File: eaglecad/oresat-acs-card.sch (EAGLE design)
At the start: 287 parts, among them J6 J-SAMTEC-TFM-120-X1-XXX-D-RA, Q10 DMP2240UDM, Q11 MOSFET-PCH-SOT23-6, Q12 MOSFET-PCH-SOT23-6, Q13 PMV45EN, Q14 PMV45EN, Q15 DMP2240UDM, Q21 MOSFET-PCH-SOT23-6, Q22 MOSFET-PCH-SOT23-6, Q23 PMV45EN, Q24 PMV45EN, Q25 DMP2240UDM, Q31 MOSFET-PCH-SOT23-6, Q32 MOSFET-PCH-SOT23-6, Q33 PMV45EN, Q34 PMV45EN, Q35 DMP2240UDM, Q6 MOSFET-PCH-SOT23-6, Q7 MOSFET-PCH-SOT23-6, Q8 PMV45EN, Q9 PMV45EN, U10 MAX4211FETE, U11 MIC842LYC5, U12 MIC842LYC5, U17 MAX7310ATE, U18 MAX4211FETE, U19 MIC842LYC5, U20 MIC842LYC5, U25 MAX7310ATE, U26 MAX4211FETE, U27 MIC842LYC5, U28 MIC842LYC5, U5 MAX7310ATE, U6 MAX4211FETE, U7 MIC842LYC5, U8 MIC842LYC5, U9 MAX7310ATE

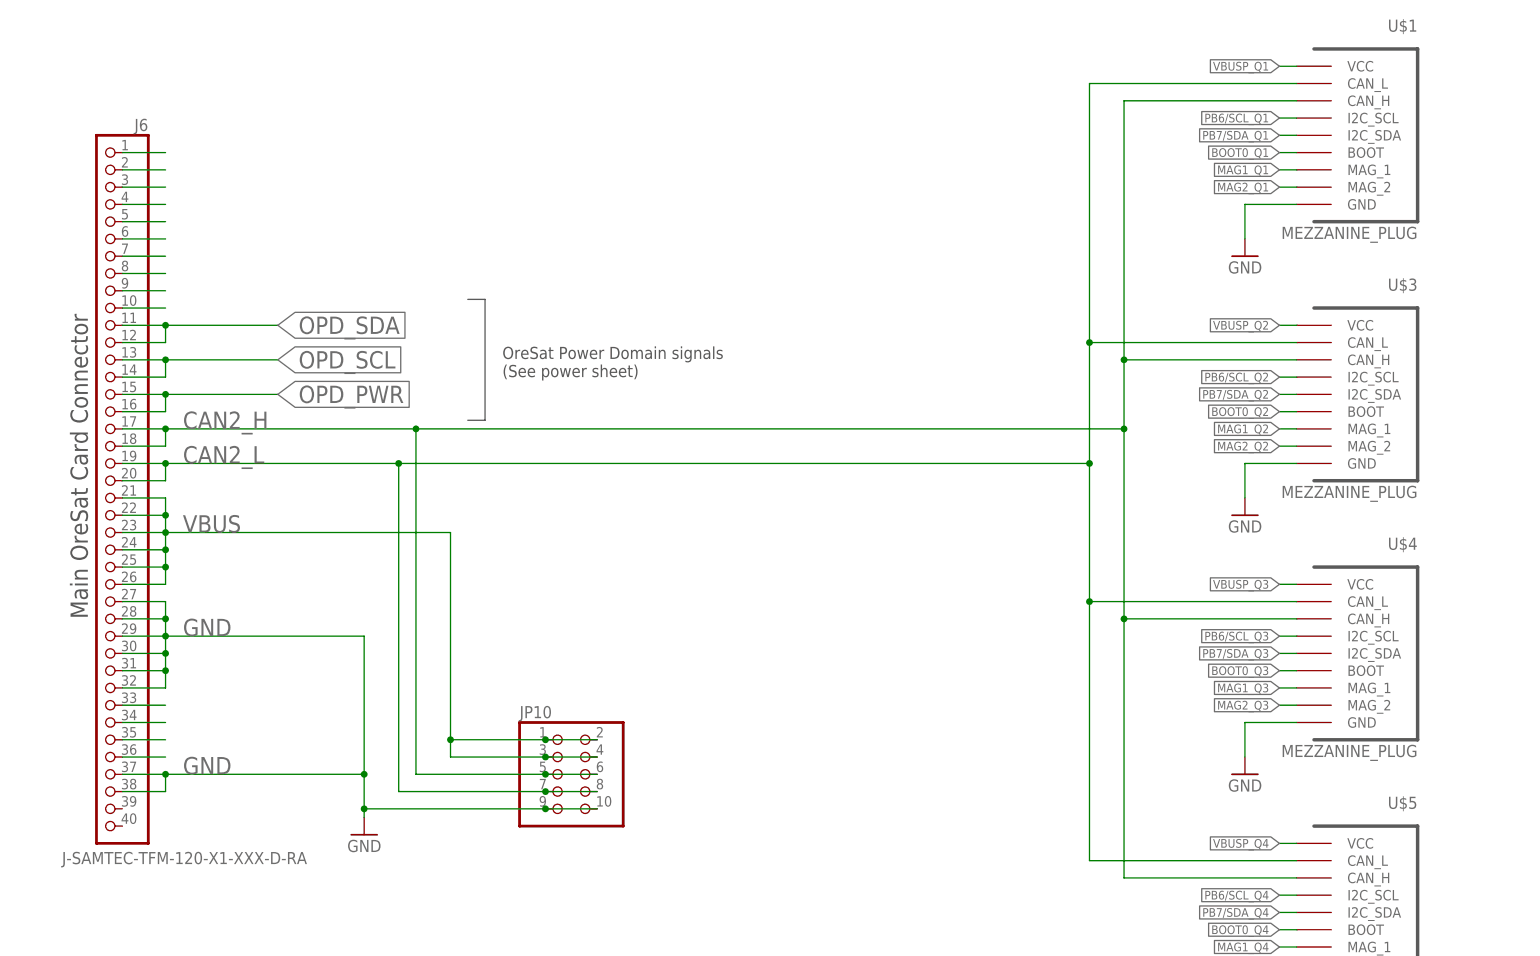
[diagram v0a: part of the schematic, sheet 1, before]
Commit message: Sanity check Eric's card. Removing supply symbols even though this is causing Andrew physical pain but EAGLE can't deal with renaming supply symbols. Also more text.
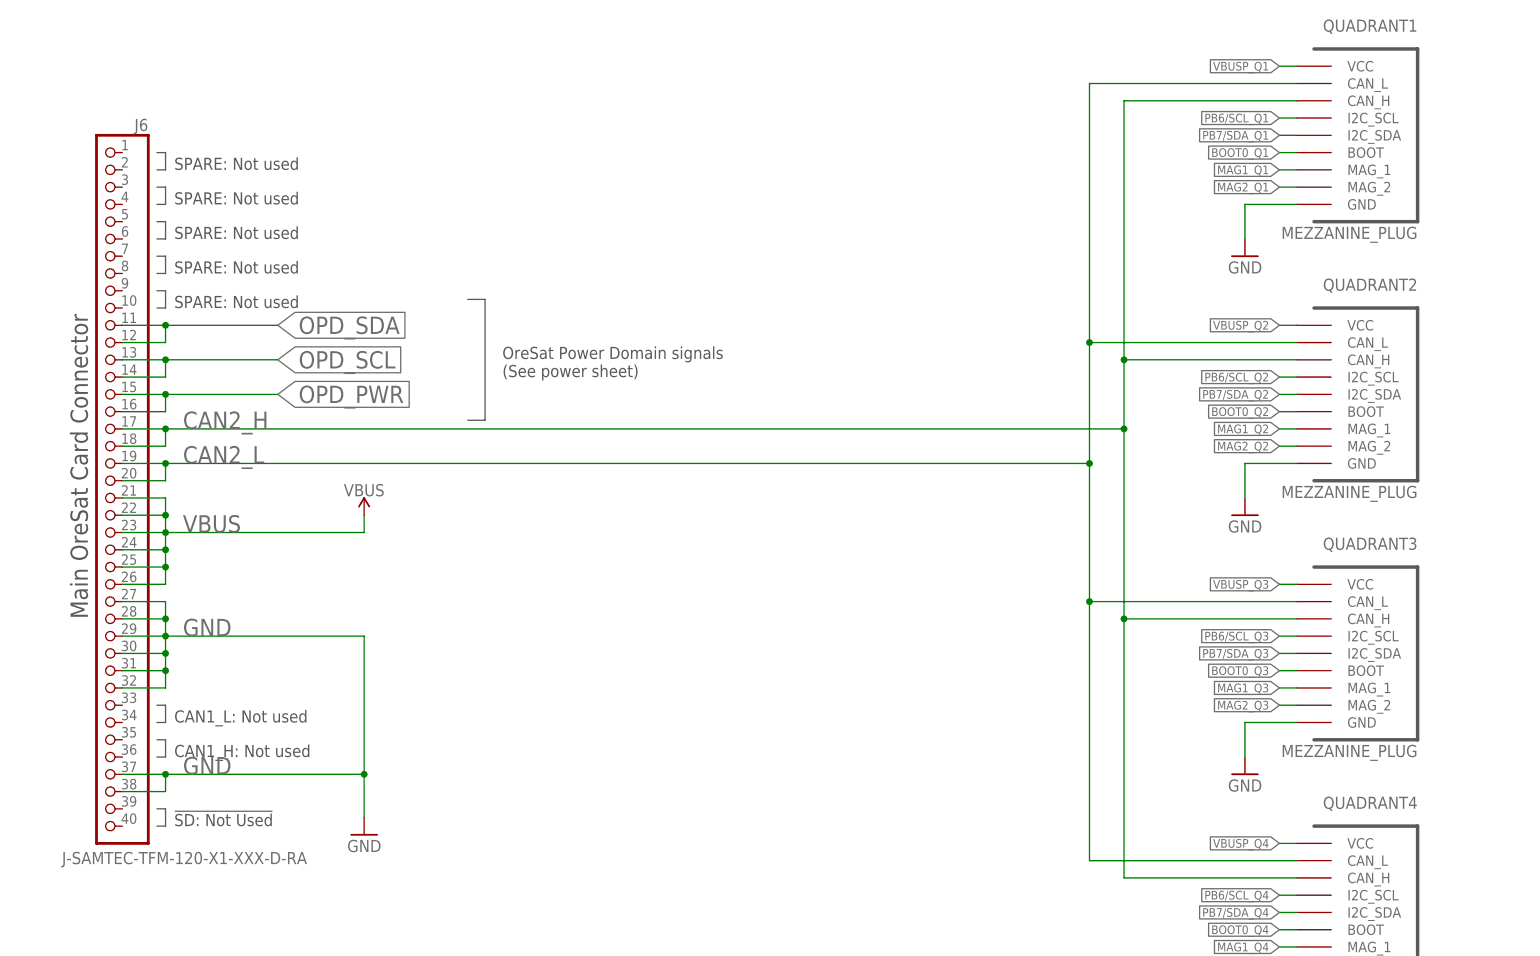
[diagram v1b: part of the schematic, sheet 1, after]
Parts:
- removed JP10: (no value), pinhead:PINHD-2X5
- renumbered U$1 to QUADRANT1, U$3 to QUADRANT2, U$4 to QUADRANT3, U$5 to QUADRANT4
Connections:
- removed net N$1: J6.34
- removed net N$271: J6.33
- removed net N$300: J6.2
- removed net N$400: J6.35
- removed net N$406: J6.36
- removed net N$479: J6.9
- removed net N$480: J6.4
- removed net N$482: J6.5
- removed net N$498: J6.1
- removed net N$499: J6.7
- removed net N$500: J6.6
- removed net N$503: J6.8
- removed net N$504: J6.10
- removed net SPARE4: J6.3
- net CAN2_H: no longer JP10.5, JP10.6
- net CAN2_L: no longer JP10.7, JP10.8
- net GND: no longer JP10.10, JP10.9
- net VBUS: no longer JP10.1, JP10.2, JP10.3, JP10.4
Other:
- note added: "!SD: Not Used"
- note added: "CAN1_H: Not used"
- note added: "CAN1_L: Not used"
- note added: "SPARE: Not used"

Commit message: Layed out power domains for four quadrants, added another power domain and an STM32F042. Also added breaker circuit and I2C buffer for Magnetometers, and an IMU
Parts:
- added C1, C16, C2, C3, C4, C46, C48, C49, C50: 1u, oresat-rcl:C-EU0603-C-NOSILK
- added C18, C26, C27, C43, C5: 100n, oresat-rcl:C-EU0603-C-NOSILK
- added C19, C20: 20p, oresat-rcl:C-EU0603-C-NOSILK
- added C44: NP, oresat-rcl:C-EU0603-C-NOSILK
- added C45: 10u, oresat-rcl:C-EU0805-B-NOSILK
- added C47: 22u, oresat-rcl:C-EU0805-B-NOSILK
- added D16, D17: GREEN, SparkFun-LED:LED-GREEN0603
- added D18, D2: AMBER, SparkFun-LED:LED-GREEN0603
- added J2: ORESAT-DEBUG-CONNECTOR-CARD, oresat-edge_connector:ORESAT-DEBUG-CONNECTOR-CARD
- added L3: 6.8u, L-ECS-MPI4040:L-ECS-MPI4040
- added MAG_PIN_Q1, MAG_PIN_Q2, MAG_PIN_Q3, MAG_PIN_Q4: (no value), pinhead:PINHD-1X2
- added Q26, Q27: MOSFET-PCH-SOT23-6, Q-MOSFET-PCH-SOT23-6:MOSFET-PCH-SOT23-6
- added Q28, Q29: PMV45EN, Tova:PMV45EN
- added Q30: DMP2240UDM, Q-MOSFET-PCH-dual-SOT23-6:MOSFET-PCH-SOT23-6
- added R1, R10, R214, R215, R216, R218, R223, R226, R227, R268, R272, R3, R4, R6: 10k, oresat-rcl:R-US_0603-C-NOSILK
- added R198, R199, R267, R5, R7, R8: 2.7k, oresat-rcl:R-US_0603-C-NOSILK
- added R2: (no value), oresat-rcl:R-US_0603-C-NOSILK
- added R200: 10, oresat-rcl:R-US_0603-C-NOSILK
- added R201, R202, R203, R204, R205, R206, R207, R208, R209, R210, R211, R212, R220, R222, R224, R225, R228: NP, oresat-rcl:R-US_0603-C-NOSILK
- added R213, R271: 100, oresat-rcl:R-US_0603-C-NOSILK
- added R217: 100m, rcl:R-US_R1206
- added R219, R221: 0, oresat-rcl:R-US_0603-C-NOSILK
- added R269, R273: 330k, oresat-rcl:R-US_0603-C-NOSILK
- added R270, R274: 1M, oresat-rcl:R-US_0603-C-NOSILK
- added TP10, TP11, TP12, TP13, TP14, TP18, TP20: TEST-POINT, Tova:TEST-POINT
- added TP106, TP107, TP108, TP109, TP110, TP111, TP112, TP113, TP114, TP115, TP116, TP117, TP118, TP119, TP120, TP121, TP89, TP90: TEST-POINT-LARGE-SQUARE, oresat-misc:TEST-POINT-LARGE-SQUARE
- added U1: MAX892LEUA+T21-0036K-L, U-Maxim-MAX892LEUA+T-power-switch:MAX892LEUA+T21-0036K-L
- added U13: BMI088, BMI088:BMI088
- added U2: LTC4300A-1, U-Linear-LTC4300A-1-2-Wire-Bus-Buffer:LTC4300A-1
- added U29: MAX7310ATE, U-Maxim-MAX7310-I2C-GPIO-expander:MAX7310
- added U3: TCAN330, TCAN330:TCAN330
- added U30: MAX4211FETE, U-Maxim-MAX4211-power-monitor:MAX4211
- added U31: TPS62111RSA, U-TI-TPS6211x-SPS-buck:TPS6211X
- added U32, U33: MIC842LYC5, U-Microchip-MIC842-Comparator:MIC842LYC5
- added U4: STM32F042K6, STM32F042K:STM32F042K6
- added X2: 16MHZ-2.5x2mm, low-gain-radio:CRYSTAL-WITH-GND
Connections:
- removed net MAX4211-3V3_Q1: C13.1, TP39.1, U10.VCC, U9.IO7
- removed net MAX4211-3V3_Q2: C23.1, TP69.1, U17.IO7, U18.VCC
- removed net MAX4211-3V3_Q3: C33.1, TP99.1, U25.IO7, U26.VCC
- removed net MAX4211-3V3_Q4: C8.1, TP24.1, U5.IO7, U6.VCC
- new net !FAULT: Q29.D, R226.1, TP109.1, U29.IO2
- new net 3.3V: C1.1, C16.1, C18.2, C26.2, C27.2, C3.1, C4.1, C47.1, C5.2, J2.VTARGET, L3.2, R1.2, R10.1, R199.2, R3.2, R7.2, R8.2, TP113.1, U1.IN, U1.IN_2, U13.CSB1, U13.PS, U13.VDD, U13.VDDIO, U2.ENABLE, U2.VCC, U3.VCC, U31.FB, U4.VDD, U4.VDDA, U4.VDDIO2
- new net AD0: R201.1, R202.2, R203.2, R204.1, U29.AD0
- new net AD1: R205.1, R206.2, R207.2, R208.1, U29.AD1
- new net AD2: R209.1, R210.2, R211.2, R212.1, U29.AD2
- new net BOOT0: R4.2, TP10.1, U29.IO5, U4.PB8-BOOT0
- new net CAN_RX: U3.RXD, U4.PA11
- new net CAN_SHDN: U3.SHDN, U4.PA10
- new net CAN_SILENT: U3.S, U4.PA9
- new net CAN_TX: U3.TXD, U4.PA12
- new net CB-RESET: R218.2, TP108.1, U29.IO4, U30.CIN2-
- new net CB_CTRL: Q26.G, Q29.G, R223.1, TP118.1, U30.COUT1, U30.COUT2, U30.LE
- new net CRYSTALIN1: C20.1, U4.PF0-OSC_IN, X2.1
- new net CRYSTALOUT1: C19.1, U4.PF1-OSC_OUT, X2.2
- new net IOUT2: R219.2, U30.IOUT
- new net MAG_!EN: R3.1, U1.!ON, U4.PB5
- new net MAG_!FAULT: R1.1, U1.!FAULT, U4.PB4
- new net MAG_PWR: C2.1, J6.5, J6.6, U1.OUT, U1.OUT_2
- new net MAG_READY: R10.2, U2.READY
- new net MAG_SCL: J6.4, U2.SCLIN
- new net MAG_SDA: J6.3, U2.SDAIN
- new net N$2: TP39.1, U9.IO7
- new net N$23: TP24.1, U5.IO7
- new net N$25: R2.2, U1.SET
- new net N$3: TP69.1, U17.IO7
- new net N$30: D2.A, R5.1
- new net N$31: J2.DEBUG-3, TP18.1
- new net N$32: J2.DEBUG-2, TP14.1
- new net N$33: J2.DEBUG-1, TP13.1
- new net N$34: J2.DEBUG-0, TP12.1
- new net N$35: J2.SWO, TP20.1
- new net N$4: TP99.1, U25.IO7
- new net N$56: D16.A, R198.1
- new net N$58: D17.A, R199.1
- new net N$59: R214.1, U29.!RESET
- new net N$61: Q27.G, Q28.D, R215.1
- new net N$62: Q27.D, R217.1, U30.RS+
- new net N$63: R219.1, R220.2, TP106.1, U30.CIN1+
- new net N$64: R221.1, R222.2, TP90.1, U30.CIN1-
- new net N$65: R221.2, U30.CIN2+, U30.REF
- new net N$66: R225.1, U30.INHIBIT
- new net N$67: C44.1, R224.2, R225.2
- new net N$68: Q26.S, R217.2, R223.2, U30.RS-
- new net N$69: D18.A, R267.1
- new net N$70: Q30.1.S, R213.2
- new net N$71: Q30.1.G, R268.2, TP120.1, U33.OUT
- new net N$72: TP119.1, U29.IO6
- new net N$73: Q30.2.S, R271.2
- new net N$74: Q30.2.G, R272.2, TP121.1, U32.OUT
- new net N$75: C50.1, R273.1, R274.1, U32.INP
- new net N$76: C49.1, R269.1, R270.1, U33.INP
- new net N$77: TP115.1, U29.IO7
- new net NRESET: J2.NRST, TP11.1, U4.NRST
- new net ON/!OFF: C48.1, Q28.G, R216.2, R267.2, TP107.1, U29.IO3, U30.VCC
- new net PA0: R5.2, U4.PA0
- new net PA2/USART2_TX: J2.CARD-RX, U4.PA2
- new net PA3/USART2_RX: J2.CARD-TX, U4.PA3
- new net PB6/SCL: R8.1, U13.SCL/SCK, U2.SCLOUT, U29.IO0, U4.PB6
- new net PB7/SDA: R7.1, U13.SDA/SDI, U2.SDAOUT, U29.IO1, U4.PB7
- new net PEN-SCL-FILT: Q30.2.D, R202.1, R206.1, R210.1, R273.2, TP116.1, U29.SCL
- new net PEN-SDA-FILT: Q30.1.D, R204.2, R208.2, R212.2, R269.2, TP117.1, U29.SDA
- new net POUT: R6.1, TP89.1, U30.POUT
- new net POUTPROT: R6.2, U4.PA8
- new net SWCLK: J2.SWCLK, U4.PA14-SWCLK
- new net SWDIO: J2.SWDIO, U4.PA13-SWDIO
- new net TPS62111-PG2: TP111.1, U31.PG
- new net TPS62111-SYNC2: R227.1, R228.2, TP112.1, U31.SYNC
- new net TPS62111_SW2: L3.1, U31.SW
- new net VBUSP: C44.2, C45.1, C46.1, J2.VBUS, Q26.D, R198.2, R227.2, TP110.1, U31.EN, U31.VIN
- new net VPD: C43.2, R200.2, R201.2, R205.2, R209.2, R214.2, R226.2, R270.2, R274.2, TP114.1, U29.V+, U32.VDD, U33.VDD
- net CAN2_H: now also U3.CANH
- net CAN2_L: now also U3.CANL
- net GND: now also C1.2, C16.2, C18.1, C19.2, C2.2, C20.2, C26.1, C27.1, C3.2, C4.2, C43.1, C45.2, C46.2, C47.2, C48.2, C49.2, C5.1, C50.2, D16.C, D17.C, D18.C, D2.C, J2.GND, J2.PAD, Q28.S, Q29.S, R2.1, R203.1, R207.1, R211.1, R216.1, R218.1, R220.1, R222.1, R224.1, R228.1, R268.1, R272.1, R4.1, U1.GND, U13.GNDA, U13.GNDIO, U13.SDO1, U13.SDO2, U2.GND, U29.GND, U3.GND, U30.GND, U31.GND, U31.LBI, U31.LBO, U32.GND, U33.GND, U4.VSS, X2.SHIELD
- net MAG1_Q1: now also MAG_PIN_Q1.1
- net MAG1_Q2: now also MAG_PIN_Q2.1
- net MAG1_Q3: now also MAG_PIN_Q3.1
- net MAG1_Q4: now also MAG_PIN_Q4.1
- net MAG2_Q1: now also MAG_PIN_Q1.2
- net MAG2_Q2: now also MAG_PIN_Q2.2
- net MAG2_Q3: now also MAG_PIN_Q3.2
- net MAG2_Q4: now also MAG_PIN_Q4.2
- net ON/!OFF_Q1: now also C13.1, U10.VCC
- net ON/!OFF_Q2: now also C23.1, U18.VCC
- net ON/!OFF_Q3: now also C33.1, U26.VCC
- net ON/!OFF_Q4: now also C8.1, U6.VCC
- net OPD_PWR: now also R200.1
- net OPD_SCL: now also R271.1
- net OPD_SDA: now also R213.1
- net VBUS: now also Q27.S, R215.2
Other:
- note added: "0805"
- note added: "1206"
- note added: "3.3V Card Switching Supply"
- note added: "CAN Transceiver"
- note added: "ECS-MPI4040R4-6R8-R"
- note added: "Emergency M0 bootstrapping over OPD I2C Address: 0b0111110x"
- note added: "Magnetometer Breaker"
- note added: "Magnetometer I2C Buffer"
- note added: "NOTE: PB6 and PB7 tied together via 2x 10k resistors @ MAX7310!"
- note added: "NRST pull-up built in"
- note added: "Power/Current draw from OPD."
- note added: "Signal is analog voltage 0-1.2V"

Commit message: Updated board to use new STM32F0 design block
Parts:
- removed C18, C26, C27, C5: 100n, oresat-rcl:C-EU0603-C-NOSILK
- removed C19, C20: 20p, oresat-rcl:C-EU0603-C-NOSILK
- removed R4, R6: 10k, oresat-rcl:R-US_0603-C-NOSILK
- removed R5: 2.7k, oresat-rcl:R-US_0603-C-NOSILK
- removed TP18, TP20: TEST-POINT, Tova:TEST-POINT
- removed U3: TCAN330, TCAN330:TCAN330
- removed U4: STM32F042K6, STM32F042K:STM32F042K6
- added C28, C29, C37, C38, C39: 100n, oresat-rcl:C-EU0603-C-NOSILK
- added C30, C36: 20p, oresat-rcl:C-EU0603-C-NOSILK
- added R11, R12: 2.7k, oresat-rcl:R-US_0603-C-NOSILK
- added R9: 10k, oresat-rcl:R-US_0603-C-NOSILK
- added TP9: TEST-POINT, Tova:TEST-POINT
- added U14: TCAN330, TCAN330:TCAN330
- added U15: STM32F091C, U-ST-STM32F091C-uC:STM32F091C
- J2: value ORESAT-DEBUG-CONNECTOR-CARD -> ORESAT-DEBUG-CONNECTOR-SOLAR; device oresat-edge_connector:ORESAT-DEBUG-CONNECTOR-CARD -> oresat-debug-connector:ORESAT-DEBUG-CONNECTOR-SOLAR
- R7: value 2.7k -> 10k; DPN A129632CT-ND -> 311-10.0KLRCT-ND; MFR TE Connectivity -> Yageo; MPN CRGCQ0402F2K7 -> RC0402FR-0710KL
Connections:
- removed net CAN_SILENT: U3.S, U4.PA9
- removed net N$30: D2.A, R5.1
- removed net POUTPROT: R6.2, U4.PA8
- new net IMU_INT1: U13.INT1, U15.PB12
- new net IMU_INT2: U13.INT2, U15.PB13
- new net IMU_INT3: U13.INT3, U15.PB15
- new net IMU_INT4: U13.INT4, U15.PB14
- new net N$37: J2.SWO, TP14.1
- new net PA1: U15.PA1
- new net PA15: U15.PA15
- new net PA4: U15.PA4
- new net PA5/SPI1_SCK: U15.PA5
- new net PA6/SPI1_MISO: U15.PA6
- new net PA7/SPI1_MOSI: U15.PA7
- new net PA8/POUTPROT: R9.2, U15.PA8
- new net PA9/CAN_SILENT: U14.S, U15.PA9
- new net PB0: U15.PB0
- new net PB1: U15.PB1
- new net PB10: U15.PB10
- new net PB11: U15.PB11
- new net PB2: U15.PB2
- new net PB8: U15.PB8
- new net PB9: U15.PB9
- new net PC13: U15.PC13
- new net PC14: U15.PC14-OSC32_IN
- new net PC15: U15.PC15-OSC32_OUT
- net 3.3V: now also C28.2, C29.2, C37.2, C38.2, C39.2, R11.2, R12.2, U14.VCC, U15.VBAT, U15.VDD, U15.VDDA, U15.VDDIO2; no longer C18.2, C26.2, C27.2, C5.2, R7.2, R8.2, U3.VCC, U4.VDD, U4.VDDA, U4.VDDIO2
- net BOOT0: now also R7.2, TP9.1, U15.PF11-BOOT0; no longer R4.2, TP10.1, U4.PB8-BOOT0
- net CAN2_H: now also U14.CANH; no longer U3.CANH
- net CAN2_L: now also U14.CANL; no longer U3.CANL
- net CAN_RX: now also U14.RXD, U15.PA11; no longer U3.RXD, U4.PA11
- net CAN_SHDN: now also U14.SHDN, U15.PA10; no longer U3.SHDN, U4.PA10
- net CAN_TX: now also U14.TXD, U15.PA12; no longer U3.TXD, U4.PA12
- net CRYSTALIN1: now also C36.1, U15.PF0-OSC_IN; no longer C20.1, U4.PF0-OSC_IN
- net CRYSTALOUT1: now also C30.1, U15.PF1-OSC_OUT; no longer C19.1, U4.PF1-OSC_OUT
- net GND: now also C28.1, C29.1, C30.2, C36.2, C37.1, C38.1, C39.1, R7.1, U14.GND, U15.VSS, U15.VSSA; no longer C18.1, C19.2, C20.2, C26.1, C27.1, C5.1, R4.1, U3.GND, U4.VSS
- net MAG_!EN: now also U15.PB4; no longer U4.PB5
- net MAG_!FAULT: now also U15.PB3; no longer U4.PB4
- net MAG_READY: now also U15.PB5
- net N$31: now also D2.A, R8.1; no longer J2.DEBUG-3, TP18.1
- net N$32: now also J2.DEBUG-3, TP13.1; no longer J2.DEBUG-2, TP14.1
- net N$33: now also J2.DEBUG-2, TP12.1; no longer J2.DEBUG-1, TP13.1
- net N$34: now also J2.DEBUG-1, TP11.1; no longer J2.DEBUG-0, TP12.1
- net N$35: now also J2.DEBUG-0, TP10.1; no longer J2.SWO, TP20.1
- net NRESET: now also U15.NRST; no longer TP11.1, U4.NRST
- net PA0: now also R8.2, U15.PA0; no longer R5.2, U4.PA0
- net PA2/USART2_TX: now also J2.CARD-TX, U15.PA2; no longer J2.CARD-RX, U4.PA2
- net PA3/USART2_RX: now also J2.CARD-RX, U15.PA3; no longer J2.CARD-TX, U4.PA3
- net PB6/SCL: now also R11.1, U15.PB6; no longer R8.1, U4.PB6
- net PB7/SDA: now also R12.1, U15.PB7; no longer R7.1, U4.PB7
- net POUT: now also R9.1; no longer R6.1
- net SWCLK: now also U15.PA14-SWCLK; no longer U4.PA14-SWCLK
- net SWDIO: now also U15.PA13-SWDIO; no longer U4.PA13-SWDIO
- net VBUSP: now also J2.VBUSP; no longer J2.VBUS
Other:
- note added: "4"
- note added: "ALL CAPS 0603 16V X5R 10% OR BETTER"
- note added: "ALL RESISTORS 0603 1% OR BETTER"
- note added: "Each VDD pin bypassed"
- note added: "IMU"
- note added: "Power/Current draw from OPD. Signal is analog voltage 0-1.2V"
- note added: "Rx-Tx switch happens on programming board"
- note added: "STM32F09X Microcontroller Design Block"
- note added: "VBAT not bypassed becase not enough room instead tied into nearest bypass cap"
- note removed: "Power/Current draw from OPD."
- note removed: "Signal is analog voltage 0-1.2V"
